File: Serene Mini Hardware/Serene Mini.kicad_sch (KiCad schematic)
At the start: 52 parts, among them J1 USB_C_Receptacle, J2 Conn_01x04_Pin, U1 AP7361C-33E, U2 AP2112K-1.8, U3 STM32H753ZITx, U4 ADXL382-1BCCZ-RL, U5 ADAU1787BCBZRL, Y1 Crystal_GND24, Y2 32.768 kHz

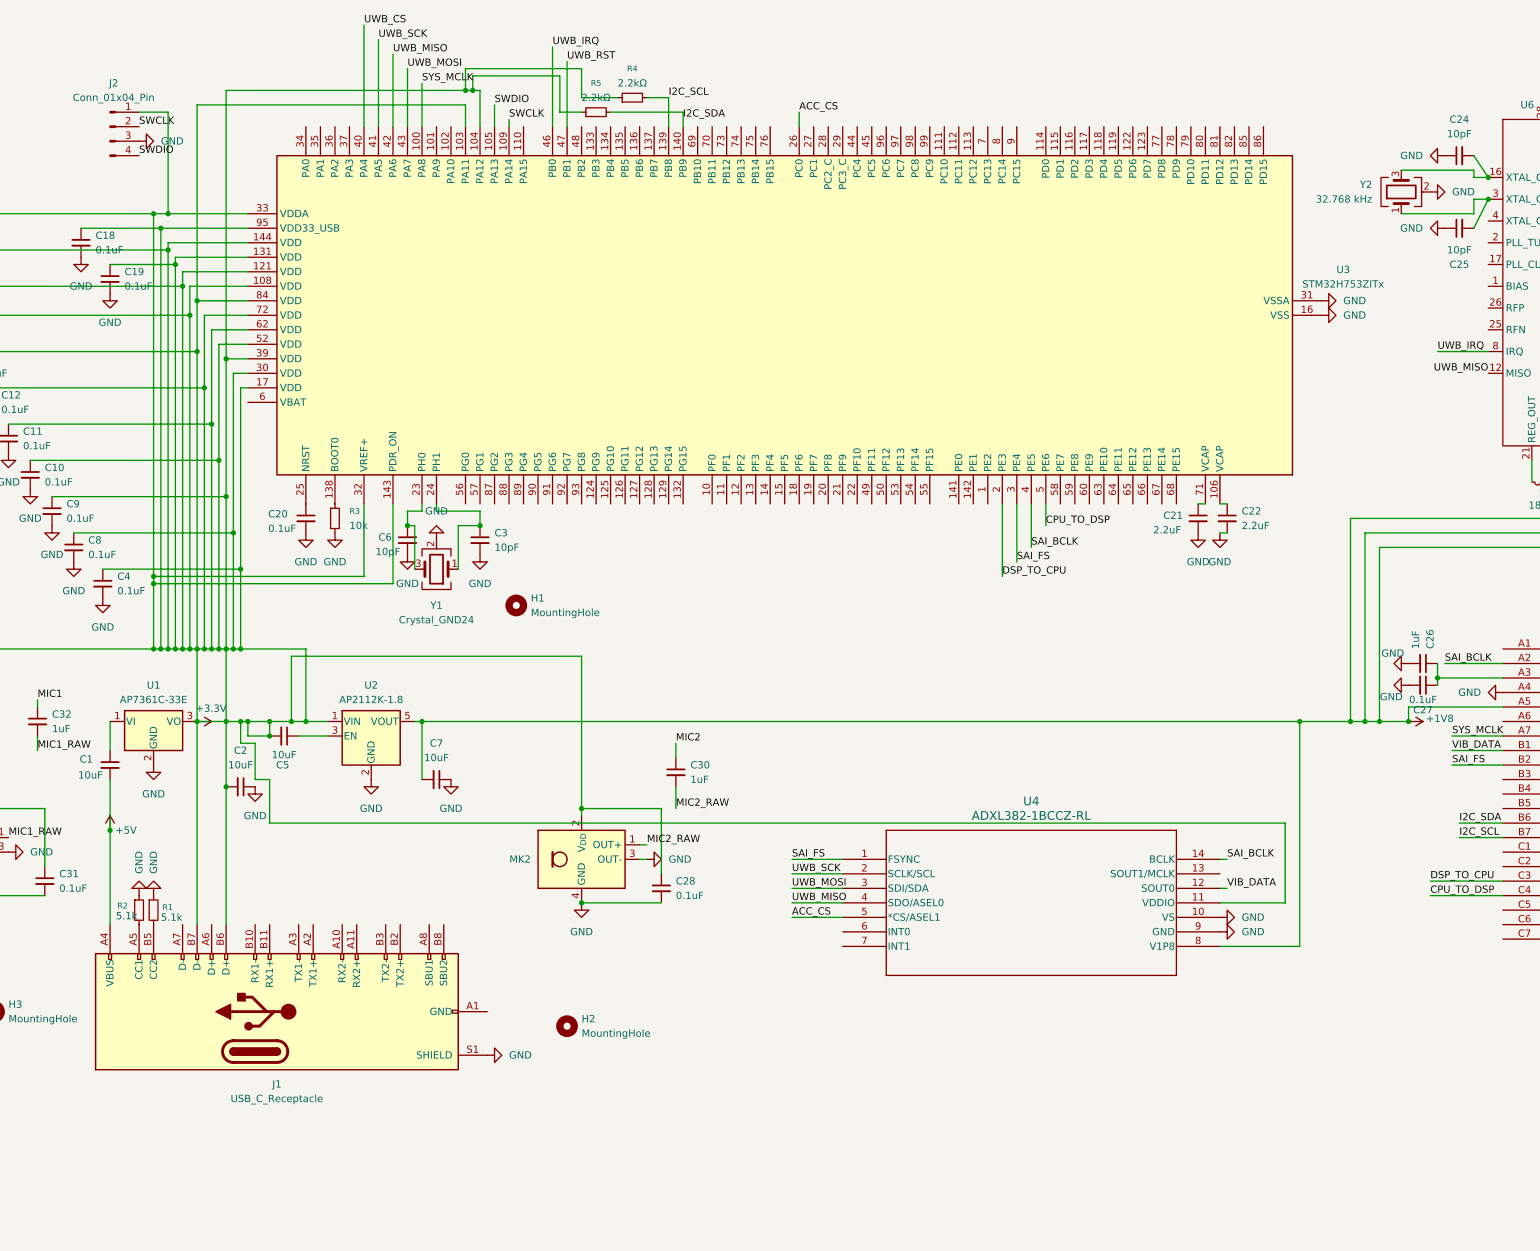
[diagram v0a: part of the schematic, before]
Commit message: Added support for battery
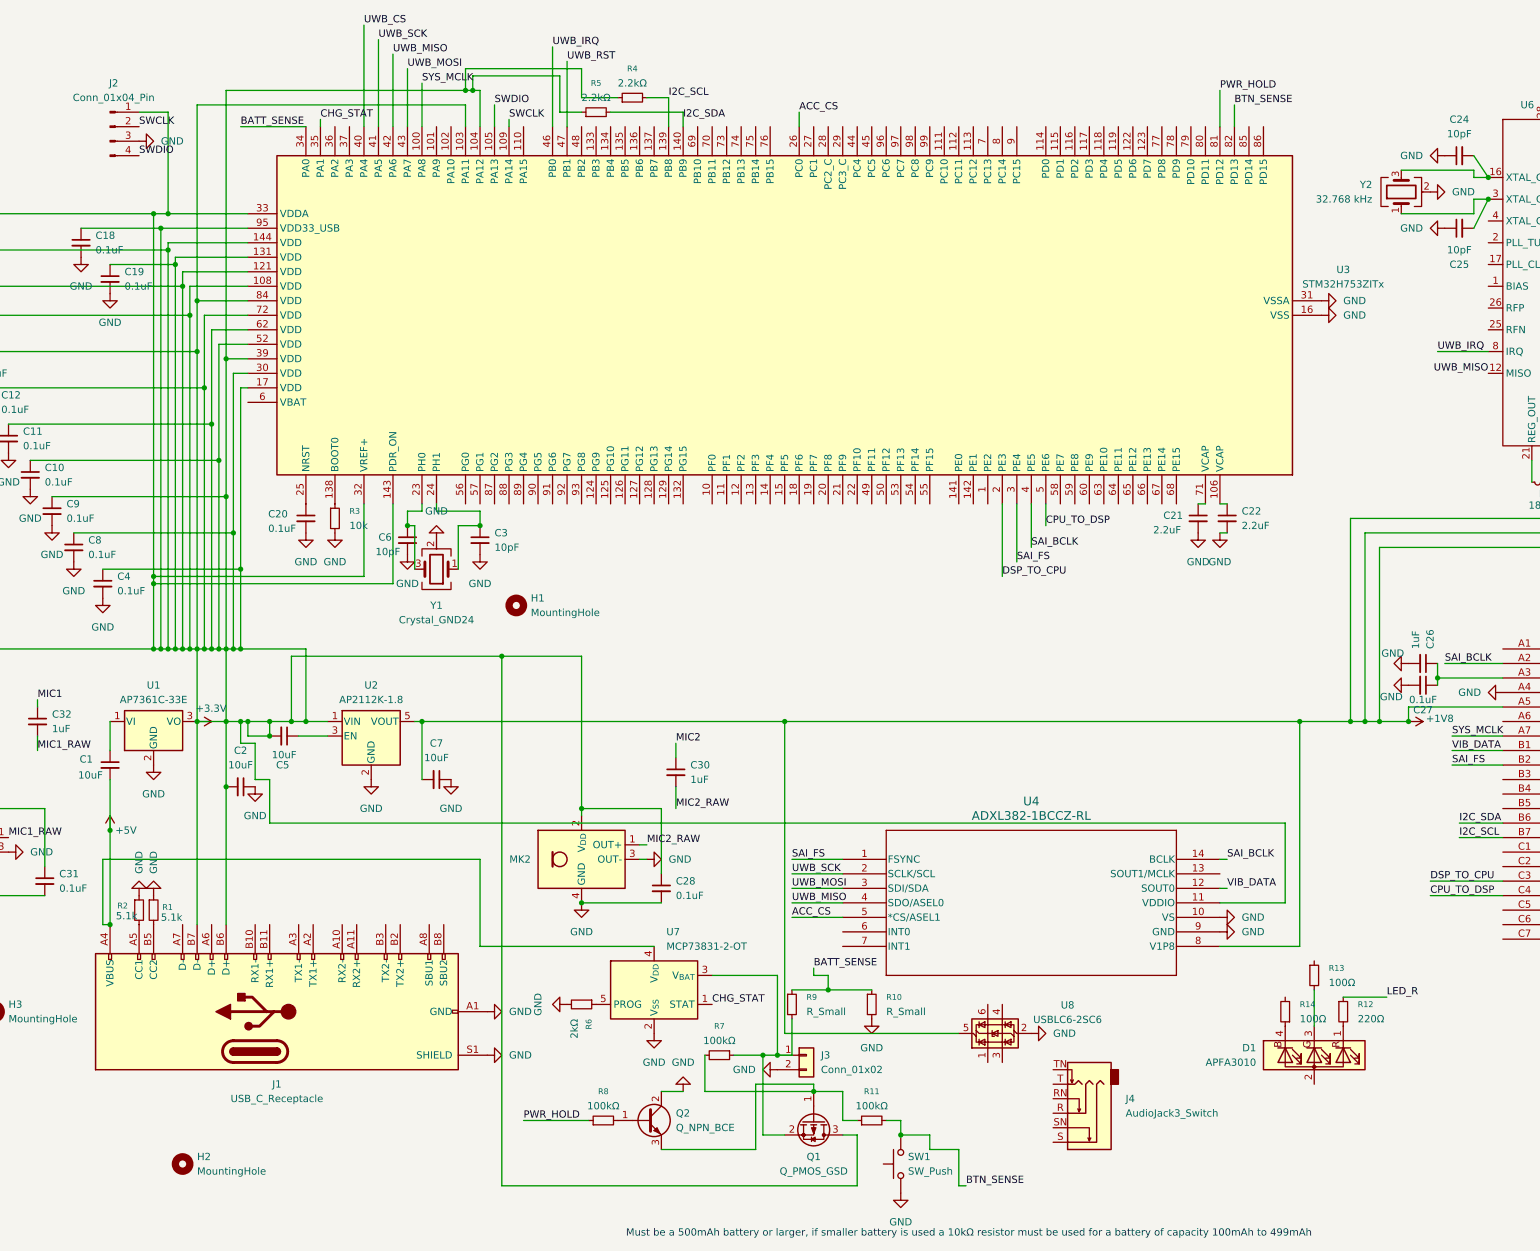
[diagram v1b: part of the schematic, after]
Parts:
- added D1: APFA3010, LED_SMD:LED_Kingbright_APFA3010_3x1.5mm_Horizontal, symbol LED:APFA3010
- added J3: Conn_01x02, symbol Connector_Generic:Conn_01x02
- added J4: AudioJack3_Switch, symbol Connector_Audio:AudioJack3_Switch
- added Q1: Q_PMOS_GSD, symbol Transistor_FET:Q_PMOS_GSD
- added Q2: Q_NPN_BCE, symbol Transistor_BJT:Q_NPN_BCE
- added R10, R9: R_Small, symbol Device:R_Small
- added R11, R7, R8: 100kΩ, symbol Device:R_Small
- added R12: 220Ω, symbol Device:R_Small
- added R13, R14: 100Ω, symbol Device:R_Small
- added R6: 2kΩ, symbol Device:R_Small
- added SW1: SW_Push, symbol Switch:SW_Push
- added U7: MCP73831-2-OT, Package_TO_SOT_SMD:SOT-23-5, symbol Battery_Management:MCP73831-2-OT
- added U8: USBLC6-2SC6, Package_TO_SOT_SMD:SOT-23-6, symbol Power_Protection:USBLC6-2SC6
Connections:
- net +1V8: now also U3.82 (PD13), R11.2, SW1.2, U8.5 (VBUS)
- net +3.3V: now also Q1.3 (D)
- net +5V: now also U7.4 (V_{DD})
- net GND: now also J1.A1 (GND), J1.A12 (GND), J1.B1 (GND), J1.B12 (GND), J3.2 (Pin_2), Q2.2 (C), R10.2, R6.2, SW1.1, U7.2 (V_{SS}), U8.2 (GND)
- net BATT_SENSE: now reaches U3.34 (PA0)
- net BATT_SENSE: now also R10.1, R9.1
- net CHG_STAT: now reaches U3.35 (PA1)
- net CHG_STAT: now also U7.1 (STAT)
- net PWR_HOLD: now reaches U3.81 (PD12)
- net PWR_HOLD: now also R8.1
- new net: Q1.1 (G), Q2.3 (E), R11.1, R7.2
- new net: Q2.1 (B), R8.2
- new net: J3.1 (Pin_1), Q1.2 (S), R7.1, R9.2, U7.3 (V_{BAT})
- new net: D1.4 (B), R14.1
- new net: R6.1, U7.5 (PROG)
- new net: D1.1 (R), R12.2
- new net: D1.3 (G), R13.2
- new net LED_R: R12.1
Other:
- note added: "Must be a 500mAh battery or larger, if smaller battery is used a 10kΩ resistor must be used for a battery of capacity 100mAh to 499mAh"
- moved on the sheet: H2

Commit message: PCB and Schematic Design Changes
Upgraded to the newer sr1120
Reduced the PCB size by ~40%
More efficient layout with chips on both side of the pcb
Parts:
- removed J1: USB_C_Receptacle, Connector_USB:USB_C_Receptacle_Amphenol_12401548E4-2A, symbol Connector:USB_C_Receptacle
- removed J2: Conn_01x04_Pin, Connector_PinHeader_2.54mm:PinHeader_1x04_P2.54mm_Vertical, symbol Connector:Conn_01x04_Pin
- removed U6: ~, ANC_Parts:Spark_SR1020_QFN28, symbol ANC_Symbols:Spark_SR1020
- added AE1: Antenna_Chip, RF_Antenna:Johanson_2450AT18x100, symbol Device:Antenna_Chip
- added C29: 1uF, Capacitor_SMD:C_0402_1005Metric, symbol Device:C_Small
- added C33, C34: 10pF, Capacitor_SMD:C_0402_1005Metric, symbol Device:C_Small
- added J5: USB_C_Receptacle_USB2.0_14P, Connector_USB:USB_C_Receptacle_GCT_USB4085, symbol Connector:USB_C_Receptacle_USB2.0_14P
- added R15: 10kΩ, Resistor_SMD:R_0402_1005Metric, symbol Device:R_Small
- added R16: 100kΩ, Resistor_SMD:R_0402_1005Metric, symbol Device:R_Small
- added T1: Transformer_1P_1S, RF_Converter:Balun_Johanson_1.6x0.8mm, symbol Device:Transformer_1P_1S
- added TP1, TP2, TP3, TP4: TestPoint, TestPoint:TestPoint_Pad_1.0x1.0mm, symbol Connector:TestPoint
- added U9: ~, ANC_Parts:Spark_SR1120_QFN32, symbol ANC_Symbols:Spark_SR1120
- D1: footprint LED_SMD:LED_Kingbright_APFA3010_3x1.5mm_Horizontal -> MountingHole:MountingHole_2mm
- H1, H2, H3: footprint MountingHole:MountingHole_2.2mm_M2 -> MountingHole:MountingHole_2.2mm_M2_DIN965_Pad
- J3: footprint (none) -> Connector_PinHeader_2.00mm:PinHeader_1x02_P2.00mm_Vertical
- J4: footprint (none) -> Connector_Audio:Jack_3.5mm_CUI_SJ2-3593D-SMT_Horizontal
- Q1, Q2: footprint (none) -> Package_TO_SOT_SMD:SOT-23
- R10, R9: value R_Small -> 100kΩ; footprint (none) -> Resistor_SMD:R_0402_1005Metric
- R11, R12, R13, R14, R6, R7: footprint (none) -> Resistor_SMD:R_0402_1005Metric
- R8: value 100kΩ -> 10kΩ; footprint (none) -> Resistor_SMD:R_0402_1005Metric
- SW1: footprint (none) -> Button_Switch_SMD:SW_Push_1P1T-SH_NO_CK_KMR2xxG
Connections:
- net BATT_SENSE is gone; now on net +1V8: R10.1, R9.1, U3.34 (PA0)
- net +1V8: now also J4.S, U5.E1 (HPGND), U5.F4 (CM), C29.1; no longer U3.82 (PD13), U5.F2 (AVDD)
- net +3.3V: now also U5.F2 (AVDD), J5.B6 (D+), J5.B7 (D-), R15.2, TP1.1, U9.21 (VDD_BAT), U9.23 (VDD_PA), U9.4 (VDD_ANA), U9.8 (VDD_REG)
- net +5V: now also J5.A4 (VBUS), J5.A9 (VBUS), J5.B4 (VBUS), J5.B9 (VBUS)
- net GND: now also D1.2 (A), AE1.1 (FEED), C29.2, J5.A1 (GND), J5.A12 (GND), J5.B1 (GND), J5.B12 (GND), J5.S1 (SHIELD), R16.1, T1.3 (SA), TP3.1; no longer U5.E1 (HPGND)
- net LED_R: now also U3.82 (PD13)
- net SWCLK: now also TP2.1
- net SWDIO: now also TP4.1
- net UWB_CS: now also U9.10 (CSN)
- net UWB_IRQ: now also U9.9 (IRQ)
- net UWB_MISO: now also U9.13 (MISO)
- net UWB_MOSI: now also U9.12 (MOSI)
- net UWB_RST: now also U9.16 (RSTN)
- net UWB_SCK: now also U9.11 (SCK)
- net at C24.2, Y2.3: now also U9.3 (XTAL_C2)
- net at L1.2: now also U9.22 (REG_OUT)
- net at C23.1: now also U9.20 (VDD_IO); no longer L1.1
- net at C25.2, Y2.1: now also U9.2 (XTAL_C1)
- net at R1.2: now also J5.B5 (CC2)
- net at U8.1 (I/O1): now also J4.T
- net at U8.3 (I/O2): now also J4.R
- net HPOUTR: now reaches U8.4 (I/O2)
- net HPOUTR: now also U5.E2 (HPOUTP0/LOUTP0)
- net HPOUTL: now reaches U8.6 (I/O1)
- net HPOUTL: now also U5.F1 (HPOUTN0/LOUTP0)
- net at R2.2: now also J5.A5 (CC1)
- net LED_B: now reaches R14.2
- net LED_B: now also U3.86 (PD15)
- net HP_DETECT: now reaches U3.115 (PD1)
- net HP_DETECT: now also J4.TN, R15.1
- net UWB_SHDN: now reaches U3.133 (PB3)
- net UWB_SHDN: now also R16.2, U9.7 (SHUTDOWN)
- net LED_G: now reaches U3.85 (PD14)
- net LED_G: now also R13.1
- new net: C34.2, T1.1 (AA)
- new net: C33.1, T1.2 (AB)
- new net: AE1.2 (PCB_Trace), T1.4 (SB)
- new net: C34.1, U9.30 (RFP)
- new net: C33.2, U9.29 (RFN)
- new net: L1.1, U9.24 (VDD_CORE_DIG), U9.27 (VDD_CORE_ANA)
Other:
- moved on the sheet: C23, C24, C25, D1, H2, H3, L1, R12, R13, R14, Y2

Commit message: Final PCB and Schematic Design
- Added new IC to support fast charging for batteries up to 3000mAh

- Added a bluetooth chip

- Used smaller coaxial ports to increase available space

- The button is now located off the board connected via molax

- Finished routing
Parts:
- removed AE1: Antenna_Chip, RF_Antenna:Johanson_2450AT18x100, symbol Device:Antenna_Chip
- removed C5: 10uF, Capacitor_SMD:C_0402_1005Metric, symbol Device:C_Small
- removed D1: APFA3010, MountingHole:MountingHole_2mm, symbol LED:APFA3010
- removed H1, H2, H3: MountingHole, MountingHole:MountingHole_2.2mm_M2_DIN965_Pad, symbol Mechanical:MountingHole
- removed Q1: Q_PMOS_GSD, Package_TO_SOT_SMD:SOT-23, symbol Transistor_FET:Q_PMOS_GSD
- removed Q2: Q_NPN_BCE, Package_TO_SOT_SMD:SOT-23, symbol Transistor_BJT:Q_NPN_BCE
- removed R13, R14: 100Ω, Resistor_SMD:R_0402_1005Metric, symbol Device:R_Small
- removed SW1: SW_Push, Button_Switch_SMD:SW_Push_1P1T-SH_NO_CK_KMR2xxG, symbol Switch:SW_Push
- removed U7: MCP73831-2-OT, Package_TO_SOT_SMD:SOT-23-5, symbol Battery_Management:MCP73831-2-OT
- added C35: 4.7µF, Capacitor_SMD:C_0402_1005Metric, symbol Device:C_Small
- added C36, C38, C39, C40: 10uF, Capacitor_SMD:C_0402_1005Metric, symbol Device:C_Small
- added C37: 47nF, Capacitor_SMD:C_0402_1005Metric, symbol Device:C_Small
- added J1, J6: Conn_Coaxial, ANC_Parts:CONN_X.FL-R-SMT-180_HIR, symbol Connector:Conn_Coaxial
- added J2: Conn_01x06_Socket, ANC_Parts:CONN_503480-0540_MOL, symbol ANC_Symbols:5034800540
- added L2: 1.5uH, Inductor_SMD:L_0603_1608Metric, symbol Device:L_Small
- added U6: BQ25620RYKR, ANC_Parts:WQFN-HR18__RYK_TEX, symbol ANC_Symbols:BQ25622RYKR
- added U7: BGM220SC12WGA2R, ANC_Parts:BGM220S_SIL, symbol ANC_Symbols:BGM220SC12WGA2R
- R11, R7: value 100kΩ -> 10kΩ
- R12: value 220Ω -> 100kΩ
- R6: value 2kΩ -> 160Ω
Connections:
- net +1V8: now also U5.F2 (AVDD); no longer C29.1, J4.S, R10.1, R11.2, R9.1, U3.34 (PA0), U5.E1 (HPGND), U5.F4 (CM)
- net +3.3V: now also R11.2, J2.1, U7.21 (VREG), U7.22 (VREGVDD); no longer C2.2, J5.B6 (D+), J5.B7 (D-), U2.1 (VIN), U3.103 (PA11), U3.104 (PA12), U5.F2 (AVDD)
- net +5V: now also U1.1 (VI), U2.1 (VIN), C36.2, C38.2, L2.2, U6.16 (SW), U6.9 (SYS); no longer C1.2, J5.A4 (VBUS), J5.A9 (VBUS), J5.B4 (VBUS), J5.B9 (VBUS)
- net ACC_CS: now also U3.13 (PF3); no longer U3.26 (PC0)
- net CHG_STAT: now also U3.110 (PA15), U6.10 (STAT); no longer U3.35 (PA1)
- net GND: now also C1.1, R12.2, R8.2, T1.5 (GND), T1.6 (GND), C35.1, C36.1, C38.1, C39.1, C40.1, J1.2 (Ext), J2.2, J2.5, J6.2 (Ext), U6.14 (CE), U6.15 (GND), U6.3 (PG)
- net I2C_SCL: now also U6.13 (SCL)
- net I2C_SDA: now also U6.12 (SDA)
- net LED_R: no longer R12.1
- net UWB_CS: now also U3.44 (PC4); no longer U3.40 (PA4)
- net UWB_IRQ: now also U3.45 (PC5); no longer U3.46 (PB0)
- net UWB_RST: now also U3.37 (PA3); no longer U3.47 (PB1)
- net UWB_SHDN: now also U3.46 (PB0); no longer U3.133 (PB3)
- net at R7.2: now also R8.1, U6.6 (TS); no longer R11.1
- net V1P8_EN: now reaches U2.3 (EN)
- net V1P8_EN: now also R12.1, U3.81 (PD12)
- net at T1.4 (SB): now also J1.1 (In)
- net at J3.1 (Pin_1), R9.2: now also C1.2, U6.8 (BAT); no longer R7.1
- net BATT_SENSE: now reaches U3.102 (PA10)
- net BATT_SENSE: now also R10.1, R9.1
- net BLT_RESET: now reaches U3.141 (PE0)
- net BLT_RESET: now also U7.35 (RESETn)
- net LED_DATA: now reaches U3.36 (PA2)
- net LED_DATA: now also J2.3
- net RX: now reaches U3.77 (PD8)
- net RX: now also U7.33 (PC05)
- net TX: now reaches U3.78 (PD9)
- net TX: now also U7.34 (PC06)
- net at R6.1: now also U6.4 (ILIM)
- net USB_DM: now reaches J5.A6 (D+)
- net USB_DM: now also J5.B6 (D+), U3.104 (PA12)
- net USB_DP: now reaches J5.A7 (D-)
- net USB_DP: now also J5.B7 (D-), U3.103 (PA11)
- removed net PWR_HOLD: R8.1, U3.81 (PD12)
- new net: R7.1, U6.5 (TS_BIAS)
- new net: C40.2, J5.A4 (VBUS), J5.A9 (VBUS), J5.B4 (VBUS), J5.B9 (VBUS), U6.18 (VBUS)
- new net: J6.1 (In), U7.3 (RF_2G4)
- new net: C37.2, L2.1
- new net: C35.2, U6.2 (REGN)
- new net: C2.2, U7.14 (DECOUPLE)
- new net: C37.1, U6.1 (BTST)
- new net: C39.2, U6.17 (PMID)
- new net BTN_SENSE: J2.4, R11.1, U3.34 (PA0), U6.7 (QON)
- new net CHG_INT: U3.35 (PA1), U6.11 (INT)
- new net CM: C29.1, J4.S, U5.E1 (HPGND), U5.F4 (CM)
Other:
- moved on the sheet: C7, J5, R1, R10, R2, R9, U2
